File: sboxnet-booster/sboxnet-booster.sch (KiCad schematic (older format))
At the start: 80 parts, among them J3 Conn_01x02_Male, J4 Conn_01x02_Male, J5 Screw_Terminal_01x04, J6 Screw_Terminal_01x04, J7 Power von externen 15V/4A Net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, SW1 Öffner, U1 L6206PSO-sboxnet, U2 L78L12_SOT89, U3 SN65HVD230, U4 l6206

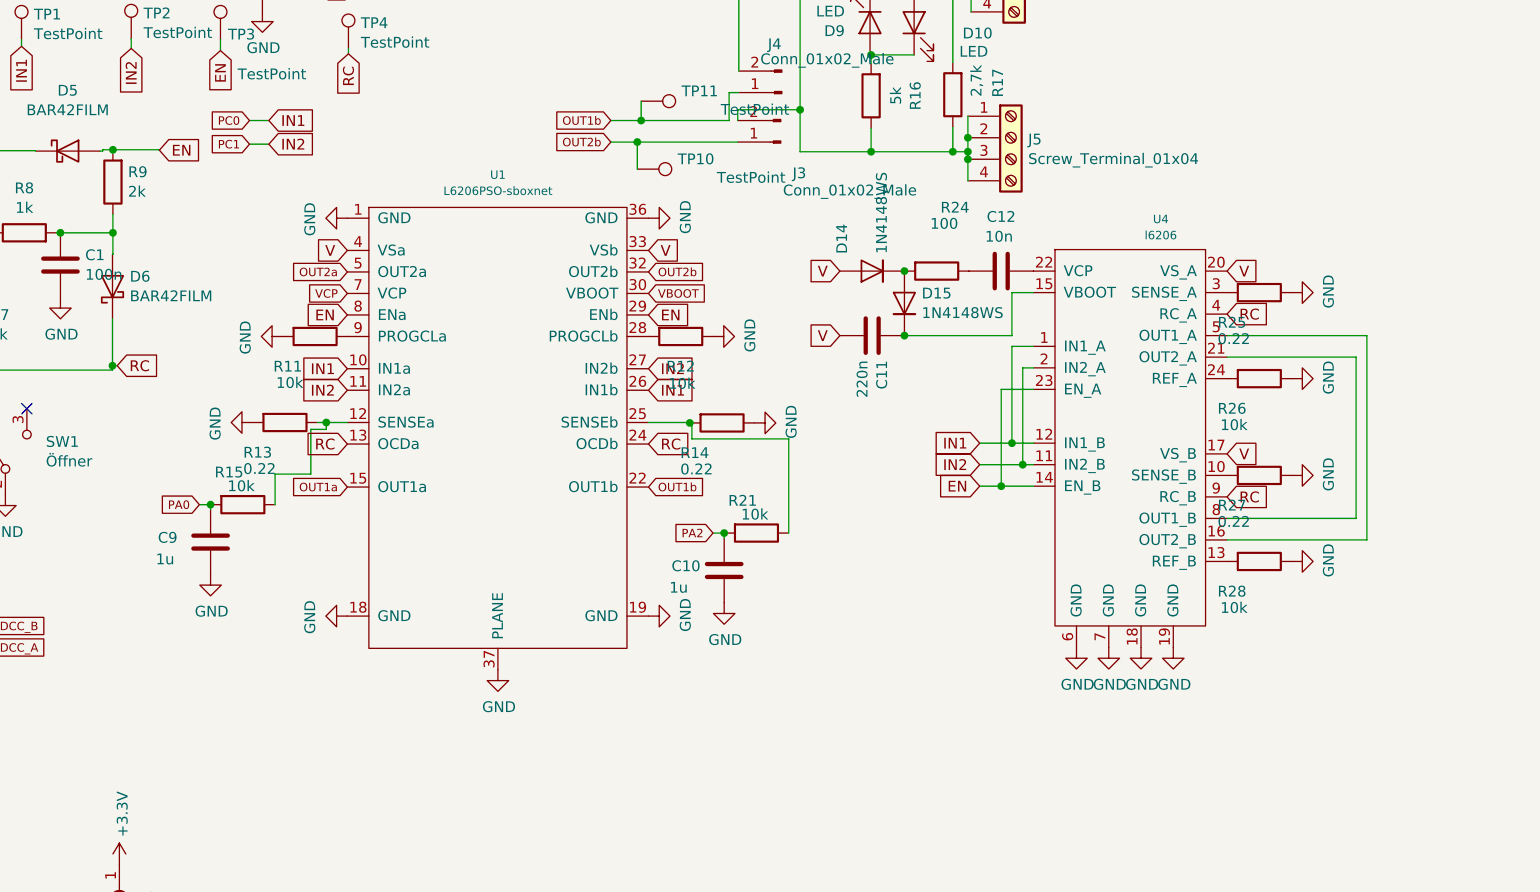
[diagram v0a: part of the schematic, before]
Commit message: booster l6206 parallel geschaltet
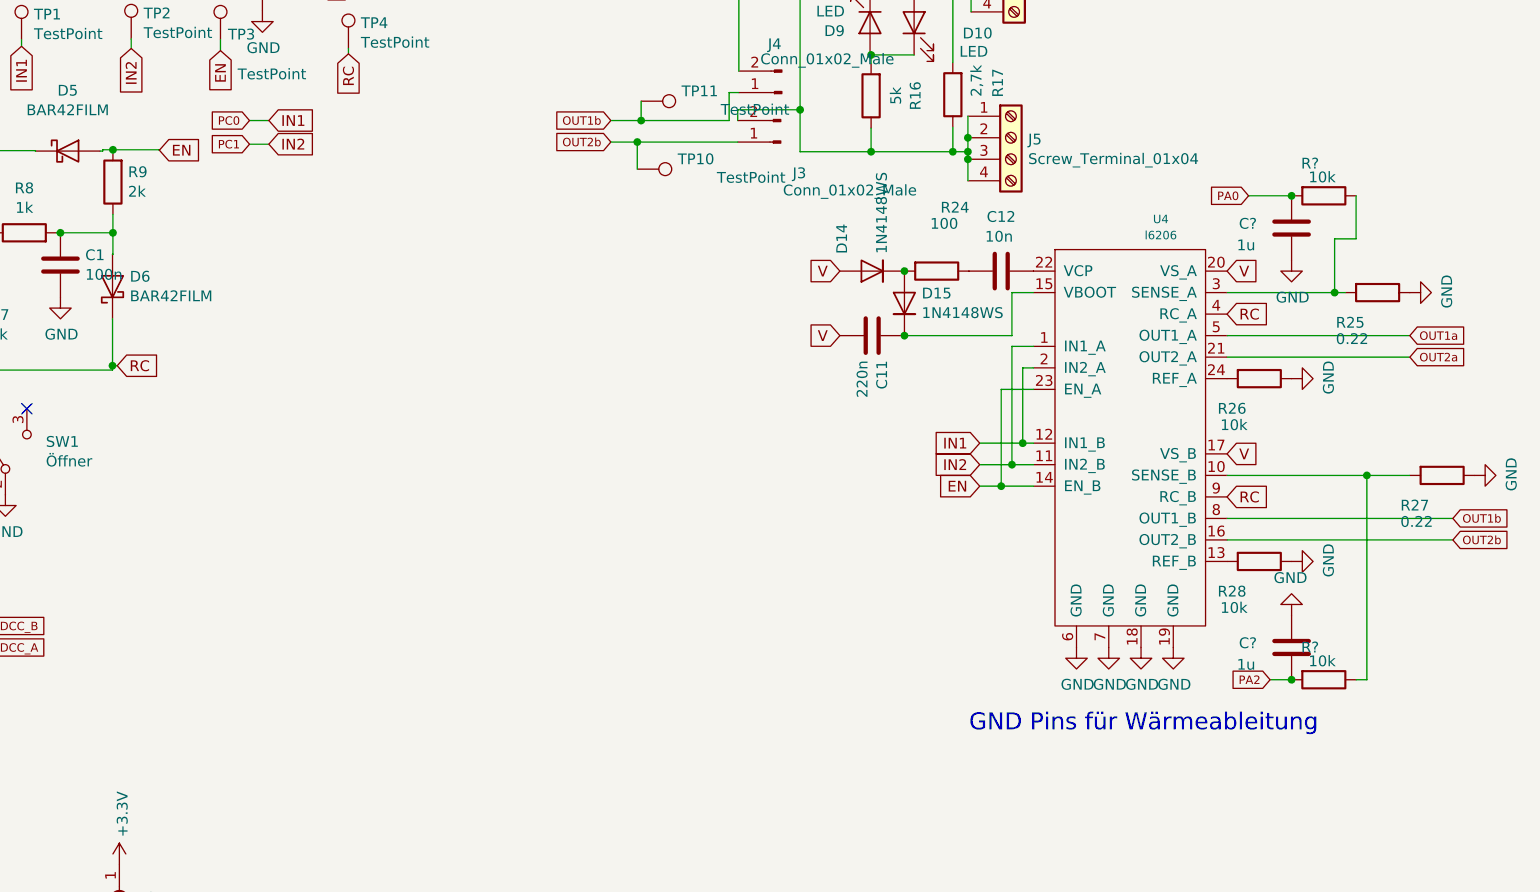
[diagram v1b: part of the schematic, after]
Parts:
- removed C10, C9: 1u, Capacitor_SMD:C_1206_3216Metric, symbol Device:C
- removed R11, R12, R15, R21: 10k, Resistor_SMD:R_1206_3216Metric, symbol Device:R
- removed R13, R14: 0.22, Resistor_THT:R_Axial_Power_L38.0mm_W9.0mm_P45.72mm, symbol Device:R
- removed U1: L6206PSO-sboxnet, sboxnet:HSOP-36-1EP_11.0x15.9mm_P0.65mm_SlugDown_ThermalVias, symbol sboxnet:L6206PSO-sboxnet
- added C? (x2): 1u, Capacitor_SMD:C_1206_3216Metric, symbol Device:C
- added R? (x2): 10k, Resistor_SMD:R_1206_3216Metric, symbol Device:R
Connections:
- wire segments 169 -> 159
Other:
- note added: "GND Pins für Wärmeableitung"
- moved on the sheet: R25, R27

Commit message: IN1 and IN2 fixed
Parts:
- removed C2: 220n, Capacitor_SMD:C_1206_3216Metric, symbol Device:C
- removed C3: 10n, Capacitor_SMD:C_1206_3216Metric, symbol Device:C
- removed D7, D8: 1N4148WS, Diode_SMD:D_SOD-323, symbol Diode:1N4148WS
- removed J7: Power von externen 15V/4A Netzteil DS_NRJ4HF, Connector_Audio:Jack_6.35mm_Neutrik_NRJ4HF_Horizontal, symbol Connector:AudioJack2
- removed R10: 100, Resistor_SMD:R_1206_3216Metric, symbol Device:R
- added C13, C14: 220n, Capacitor_SMD:C_1206_3216Metric, symbol Device:C
- added J2: cliff_FCR681465P_audiobuchse, sboxnet:CLIFF-FCR681465P, symbol sboxnet:cliff_FCR681465P_audiobuchse
- C7: value 1000u -> 2700u/25v; footprint Capacitor_THT:CP_Radial_D12.5mm_P5.00mm -> Capacitor_THT:CP_Radial_D16.0mm_P7.50mm
- C8: value 47u -> 22u/50v
- D11: value LED gn -> LED Power (gn)
- J1: renamed from J?; footprint (none) -> sboxnet:sboxnet-stecker-2x17
- JP1, JP2, JP3: renamed from JP?; footprint (none) -> Jumper:SolderJumper-3_P1.3mm_Open_RoundedPad1.0x1.5mm
- U4: footprint (none) -> Package_DIP:DIP-24_W10.16mm
- gave numbers to parts that had none: 4
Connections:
- net VBOOT is gone; now on an unnamed net: TP8.1
- net DCC_A: now also J1.33 (Pin_33)
- net GND: now also C13.1, C14.1, J2.3 (T)
- net IN1: now also U4.1 (IN1_A), U4.11 (IN2_B); no longer U4.12 (IN1_B), U4.2 (IN2_A)
- net IN2: now also U4.12 (IN1_B), U4.2 (IN2_A); no longer U4.1 (IN1_A), U4.11 (IN2_B)
- net PD0: now also J1.25 (Pin_25)
- net PD2: now also J1.27 (Pin_27)
- net V: now also C13.2, C14.2
- net at D12.2 (A): now also J2.1 (S)
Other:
- note added: "Booster 5 101"
- moved on the sheet: C6, C7, D12, TP7, TP8
